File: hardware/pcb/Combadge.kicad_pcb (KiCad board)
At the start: 2 copper layers, 33.7 x 31 mm, 32 parts, among them J1 Conn_01x02_Female, J2 USB_B_Micro, J3 TOUCH, J4 Conn_01x02_Female, SW1 CSS-1210TB, U1 XC6808A4D28R-G, U2 ESP32-WROOM-32, U3 NCP160AMX330TBG, U4 MAX98357AEWL+T, U5 RN4989

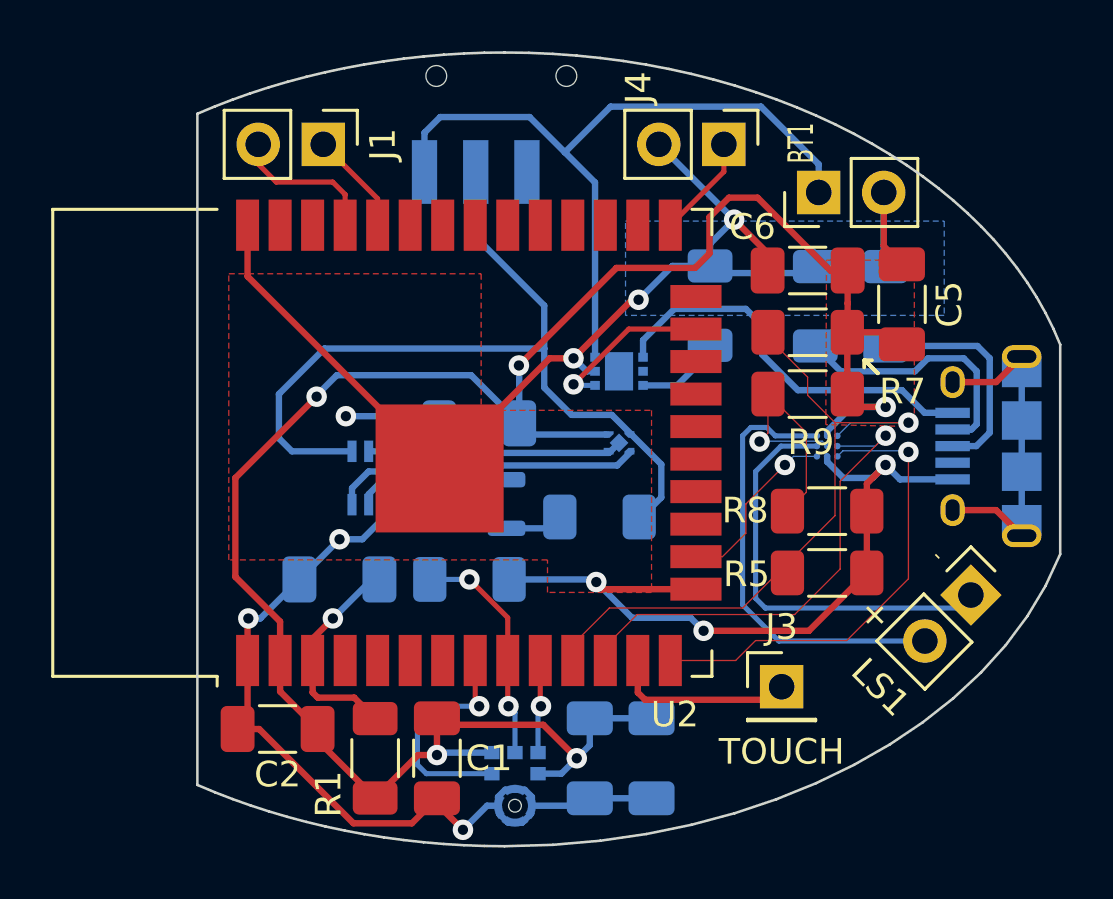
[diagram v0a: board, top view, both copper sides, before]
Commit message: Fix USP-6B07 footprint
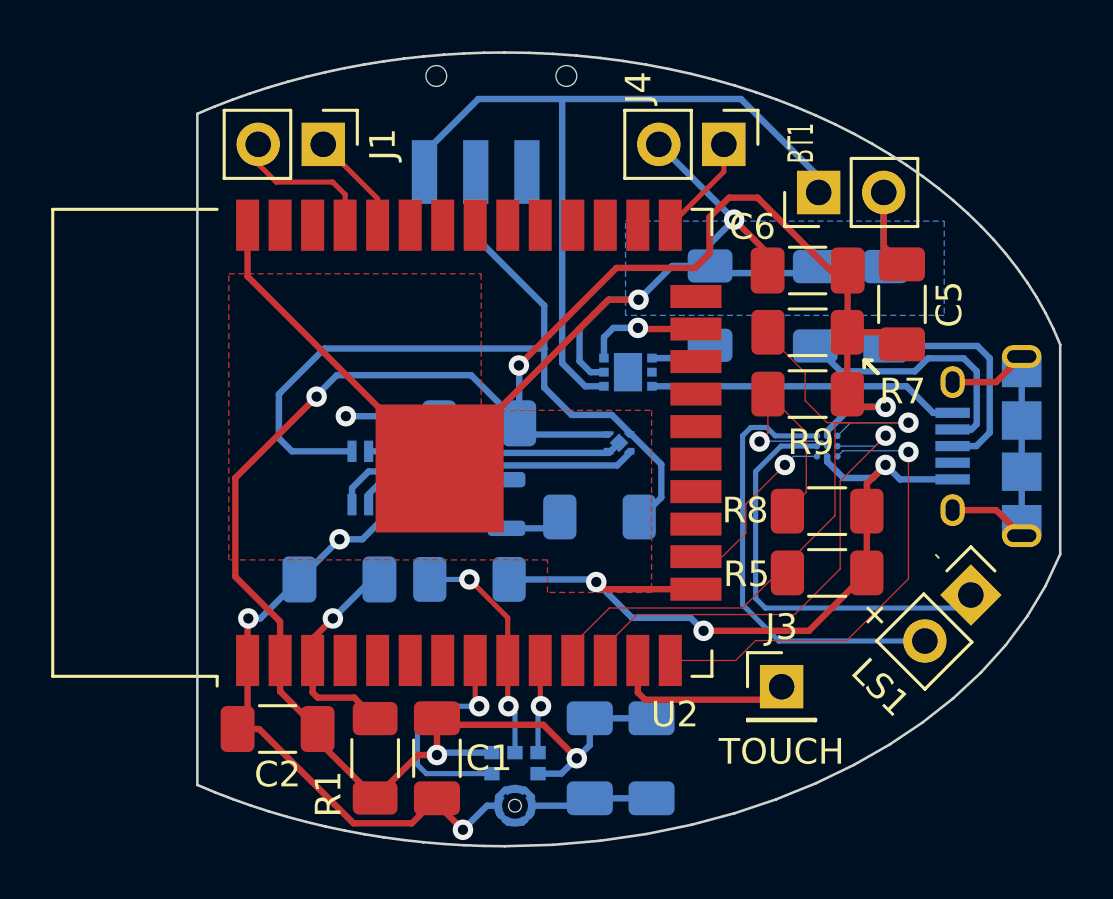
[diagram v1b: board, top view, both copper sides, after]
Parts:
- moved U1 0.35 mm to (160.8, 92.8), turned to 90 degrees
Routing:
- net GND: track 127.1 -> 131.2 mm, vias 10 -> 9
- net Net-(J2-Pad1): track 15.6 -> 12.2 mm
- net +BATT: track 29.0 -> 31.2 mm
- net /Power/CHRG_STATUS: track 6.53 -> 4.57 mm
- net /SPK_EN: track 27.3 -> 28.3 mm
- net Net-(R_ISET1-Pad2): track 3.15 -> 2.48 mm
- removed copper zone on F.Cu, net +3.3V

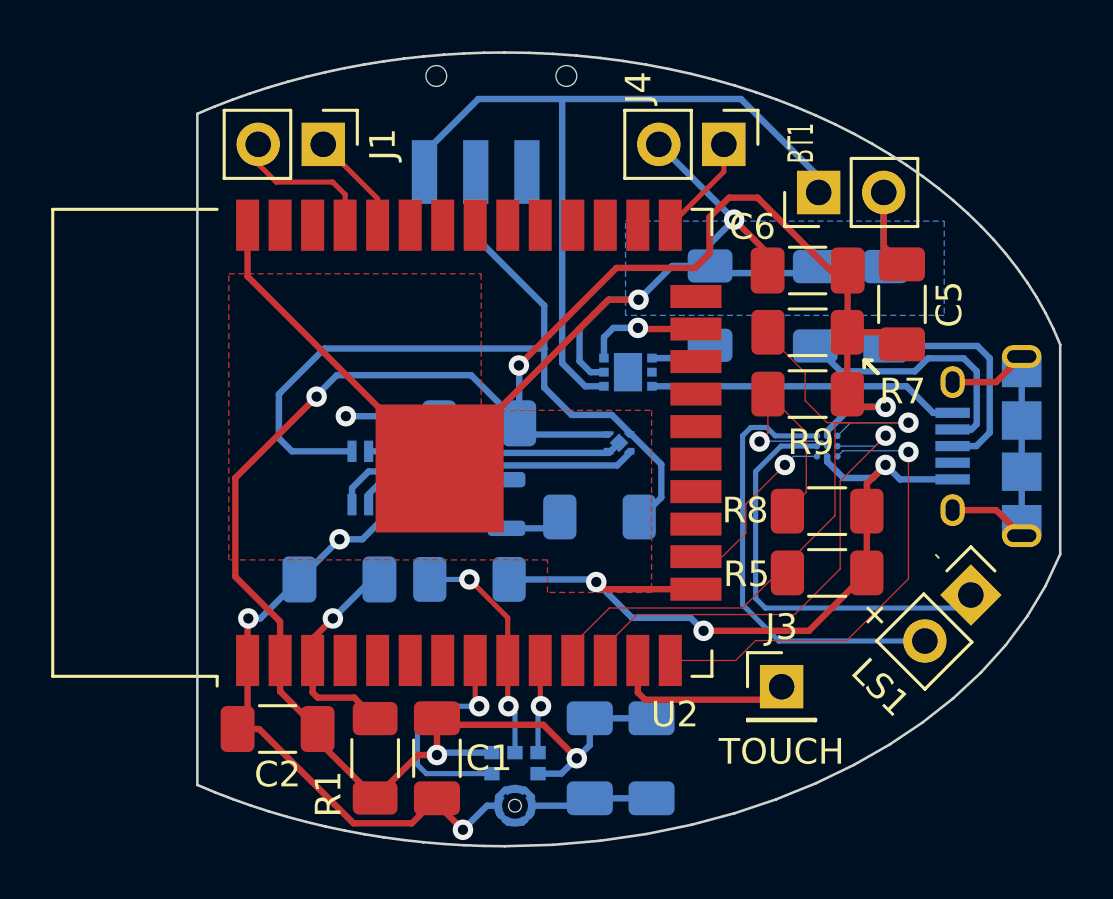
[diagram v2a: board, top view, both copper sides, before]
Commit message: Add MCP73831 to PCB
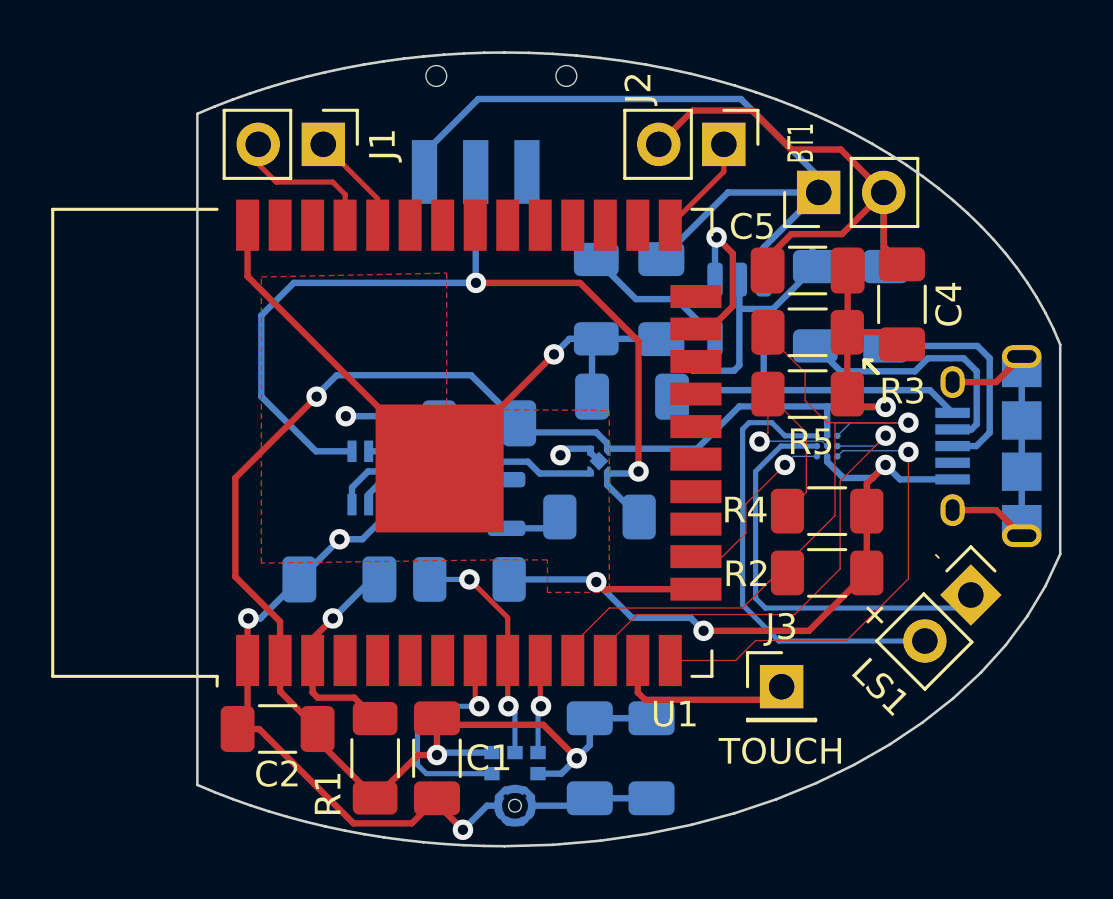
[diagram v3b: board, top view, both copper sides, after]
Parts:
- removed R_ISET1: 10k, Resistor_SMD:R_1206_3216Metric_Pad1.30x1.75mm_HandSolder
- removed the U1 at (160.8, 92.8)
- added C10: 4.7uF, Capacitor_SMD:C_1206_3216Metric_Pad1.33x1.80mm_HandSolder, B.Cu at (162.1, 89.9)
- added C9: 4.7uF, Capacitor_SMD:C_1206_3216Metric_Pad1.33x1.80mm_HandSolder, B.Cu at (160.9, 93.7)
- added R9: 4k, Resistor_SMD:R_1206_3216Metric_Pad1.30x1.75mm_HandSolder, B.Cu at (159.5, 89.9)
- added U3: MCP73831-2-OT, Package_TO_SOT_SMD:SOT-23-5, B.Cu at (165.1, 90.3)
- moved U5 1.06 mm to (159.6, 96.2), turned to 180 degrees
- renumbered C5 to C4, C6 to C5, C7 to C6, C8 to C7, C4 to C8, J4 to J2, J2 to J4, R4 to R10, R5 to R2, R7 to R3, R8 to R4, R9 to R5, R2 to R7, R3 to R8, U2 to U1, U4 to U2, U5 to U4, U3 to U5
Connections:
- net Net-(U4-GAIN_SLOT) renamed /GAIN_SELECT
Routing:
- net +3.3V: track 82.2 -> 72.6 mm, vias 5 -> 4
- net Net-(U3-PROG): track 0.00 -> 5.91 mm
- net Net-(U4-EMITTER2): track 33.7 -> 36.7 mm, vias 0 -> 2
- net Net-(U1-ISET): track 2.48 -> 0.00 mm
- net /Power/CHRG_STATUS: track 4.57 -> 6.44 mm
- net GND: track 131.2 -> 133.0 mm
- net Net-(U4-COLLECTOR2): track 12.2 -> 10.6 mm
- net Net-(J4-VBUS): track 12.2 -> 13.5 mm
- net +BATT: track 31.2 -> 30.4 mm
- removed copper zone on B.Cu, net GND

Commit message: Use single resistor for setting amplifier gain
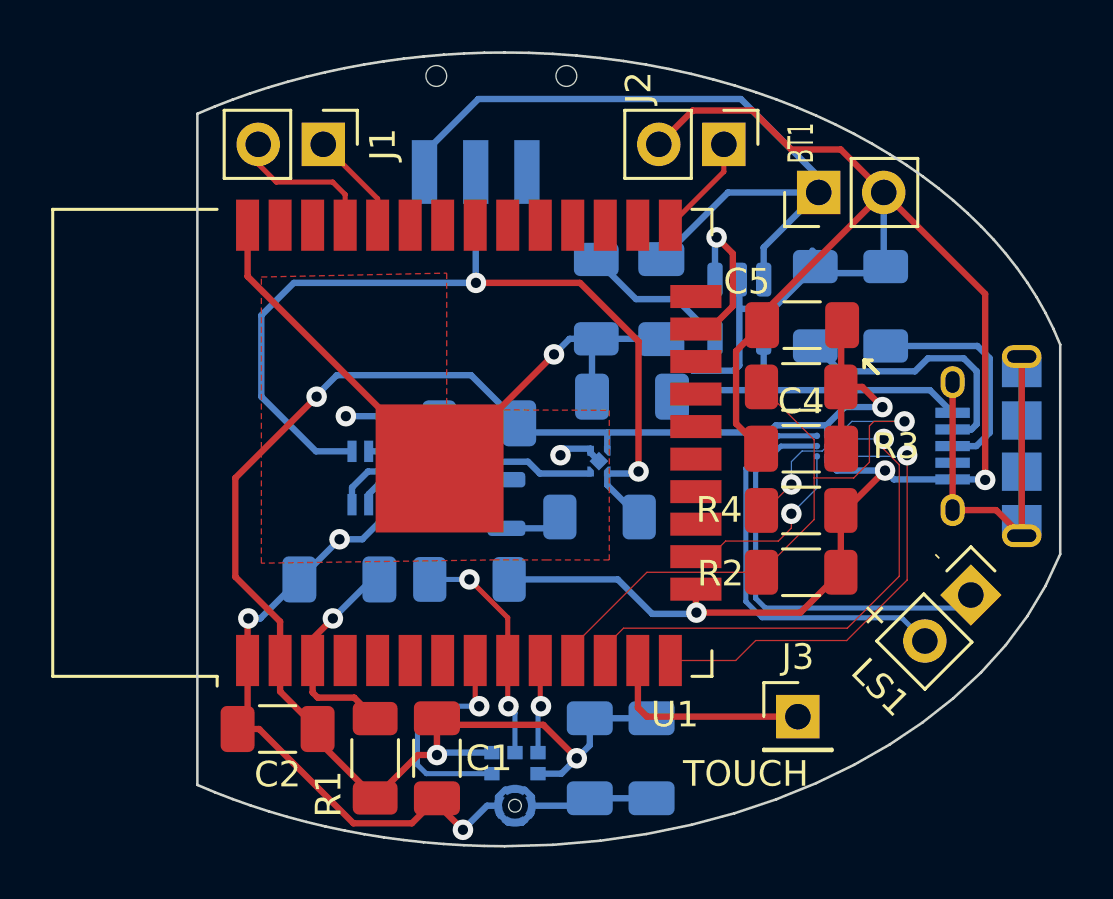
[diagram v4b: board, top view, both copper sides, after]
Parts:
- removed the R5 at (167.8, 93.6)
- R4: value TBD -> 100k
- moved C4 6.88 mm to (167.5, 95.8), turned to 0 degrees
- moved R3 2.15 mm to (167.5, 93.3)
- moved C5 2.14 mm to (167.6, 90.9)
- moved J3 1.33 mm to (167.4, 106.2)
- moved R2 1.02 mm to (167.5, 100.6)
- moved R4 1.02 mm to (167.5, 98.2)
- renumbered C8 to C10, C9 to C8, C10 to C9, R6 to R5, R7 to R6, R8 to R7, R9 to R8, R10 to R9
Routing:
- net GND: track 133.0 -> 146.1 mm
- net unconnected-(J4-Shield-Pad6): track 12.0 -> 20.9 mm
- net /GAIN_SELECT: track 10.2 -> 4.13 mm
- net +3.3V: track 72.6 -> 69.6 mm
- net /SPK_EN: track 28.3 -> 26.2 mm
- net /SPK_DATA: track 19.0 -> 20.7 mm
- net /SPK+: track 17.8 -> 16.1 mm
- net Net-(J3-Pin_1): track 7.19 -> 8.23 mm

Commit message: Cleanup silkscreen
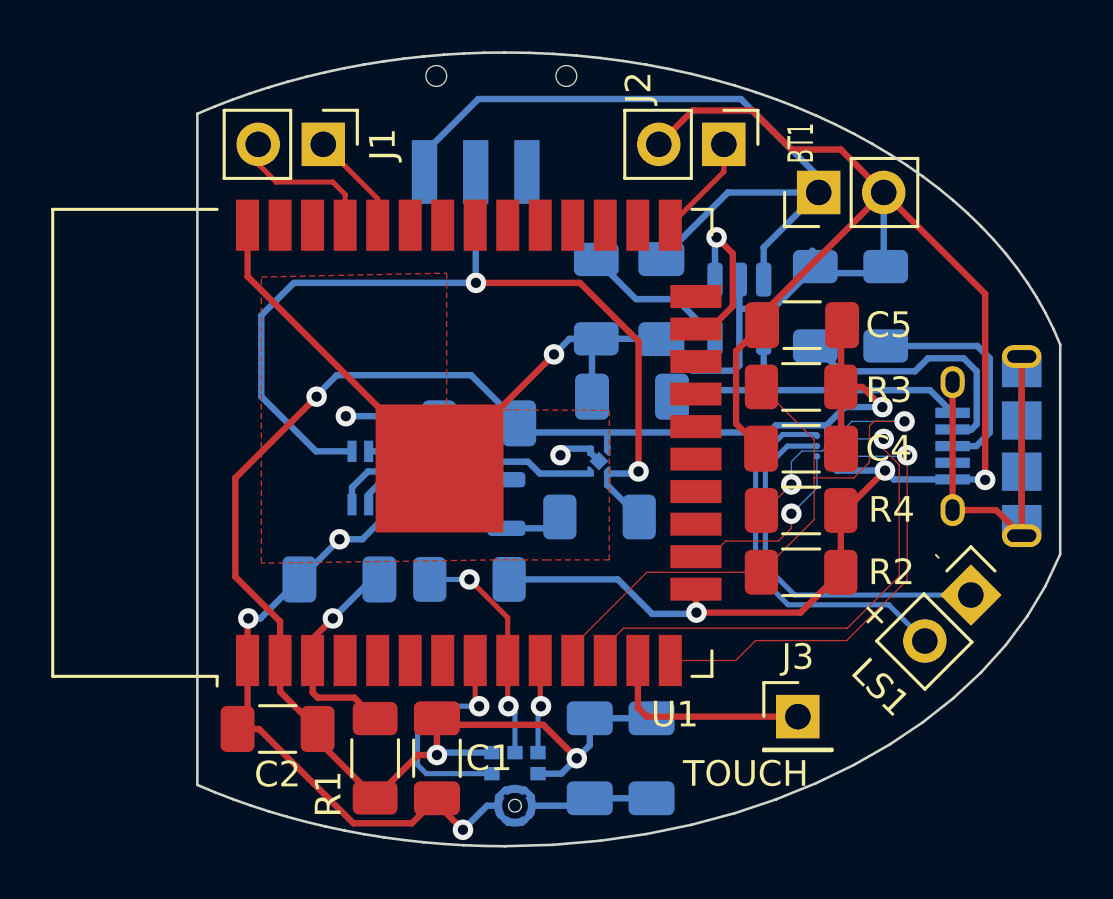
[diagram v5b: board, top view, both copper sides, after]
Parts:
- U2: value MAX98357AEWL+T -> MAX98357
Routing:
- net /SPK+: track 16.1 -> 14.9 mm
- net /SPK-: track 16.5 -> 15.4 mm
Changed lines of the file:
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@@
     (property "ki_keywords" "cap capacitor")
     (attr smd)
-    (fp_text reference "C4" (at 0 -1.85) (layer "F.SilkS")
+    (fp_text reference "C4" (at 3.429 0) (layer "F.SilkS")
         (effects (font (size 1 1) (thickness 0.15)))
     )
@@
     (property "ki_keywords" "R res resistor")
     (attr smd)
-    (fp_text reference "R3" (at -3.7084 -2.3114) (layer "F.SilkS")
+    (fp_text reference "R3" (at -3.429 -0.127) (layer "F.SilkS")
         (effects (font (size 1 1) (thickness 0.15)))
     )
@@
     (property "ki_keywords" "cap capacitor")
     (attr smd)
-    (fp_text reference "C5" (at -2.159 -1.7018) (layer "F.SilkS")
+    (fp_text reference "C5" (at 3.3905 0) (layer "F.SilkS")
         (effects (font (size 1 1) (thickness 0.15)))
     )
@@
     (property "ki_keywords" "R res resistor")
     (attr smd)
-    (fp_text reference "R4" (at -3.2004 -0.0254) (layer "F.SilkS")
+    (fp_text reference "R4" (at 3.5306 -0.0254) (layer "F.SilkS")
         (effects (font (size 1 1) (thickness 0.15)))
     )
@@
     (property "ki_keywords" "R res resistor")
     (attr smd)
-    (fp_text reference "R2" (at 3.1496 -0.0508) (layer "F.SilkS")
+    (fp_text reference "R2" (at -3.5306 0) (layer "F.SilkS")
         (effects (font (size 1 1) (thickness 0.15)))
     )
@@
     (property "ki_keywords" "cap capacitor")
     (attr smd)
-    (fp_text reference "C9" (at 0 1.85 90) (layer "B.SilkS")
-        (effects (font (size 1 1) (thickness 0.15)) (justify mirror))
+    (fp_text reference "C9" (at -2.921 -1.143 90) (layer "B.SilkS")
+        (effects (font (size 0.5 0.5) (thickness 0.125)) (justify mirror))
     )
     (fp_text value "4.7uF" (at 0 -1.85 90) (layer "B.Fab")
@@
     (property "ki_keywords" "battery charger lithium")
     (attr smd)
-    (fp_text reference "U3" (at 0 2.4 90) (layer "B.SilkS")
+    (fp_text reference "U3" (at 2.9265 0 90) (layer "B.SilkS")
         (effects (font (size 1 1) (thickness 0.15)) (justify mirror))
     )
@@
     (property "ki_keywords" "R res resistor")
     (attr smd)
-    (fp_text reference "R7" (at 0 -1.824 90) (layer "B.SilkS")
-        (effects (font (size 1 1) (thickness 0.15)) (justify mirror))
+    (fp_text reference "R7" (at -3.0226 0.081 90) (layer "B.SilkS")
+        (effects (font (size 0.5 0.5) (thickness 0.125)) (justify mirror))
     )
     (fp_text value "10k" (at 0 -1.82 90) (layer "B.Fab")
@@
     (property "ki_keywords" "cap capacitor")
     (attr smd)
-    (fp_text reference "C8" (at 0 1.85) (layer "B.SilkS")
-        (effects (font (size 1 1) (thickness 0.15)) (justify mirror))
+    (fp_text reference "C8" (at -2.794 -1.397) (layer "B.SilkS")
+        (effects (font (size 0.5 0.5) (thickness 0.125)) (justify mirror))
     )
     (fp_text value "4.7uF" (at 0 -1.85) (layer "B.Fab")
@@
         (effects (font (size 1 1) (thickness 0.15)) (justify mirror))
     )
-    (fp_text value "MAX98357AEWL+T" (at 0 -1.3462) (layer "B.SilkS")
+    (fp_text value "MAX98357" (at 0 -1.3462) (layer "B.SilkS")
         (effects (font (size 0.4 0.4) (thickness 0.05)) (justify mirror))
     )
@@
     (property "ki_keywords" "R res resistor")
     (attr smd)
-    (fp_text reference "R6" (at -1.1176 1.566 90) (layer "B.SilkS")
+    (fp_text reference "R6" (at 0.0254 1.905 90) (layer "B.SilkS")
         (effects (font (size 1 1) (thickness 0.15)) (justify mirror))
     )
@@
     (property "Sheetname" "Power")
     (attr smd)
-    (fp_text reference "U5" (at 0.04 1.778) (layer "B.SilkS")
+    (fp_text reference "U5" (at -1.928 -0.023) (layer "B.SilkS")
         (effects (font (size 1 1) (thickness 0.15)) (justify mirror))
     )
@@
     (property "ki_keywords" "R res resistor")
     (attr smd)
-    (fp_text reference "R8" (at 0 1.82 90) (layer "B.SilkS")
+    (fp_text reference "R8" (at 0 1.778 90) (layer "B.SilkS")
         (effects (font (size 1 1) (thickness 0.15)) (justify mirror))
     )
@@
     )
   )
-  (gr_line (start 170.0022 92.3036) (end 170.5102 92.8116)
-    (stroke (width 0.15) (type solid)) (layer "F.SilkS"))
-  (gr_line (start 170.5102 92.8116) (end 170.0022 92.3036)
-    (stroke (width 0.15) (type solid)) (layer "F.SilkS"))
-  (gr_line (start 169.9768 92.3036) (end 170.2816 92.3036)
-    (stroke (width 0.15) (type solid)) (layer "F.SilkS"))
-  (gr_line (start 169.9768 92.3036) (end 169.9768 92.583)
-    (stroke (width 0.15) (type solid)) (layer "F.SilkS"))
   (gr_poly
     (pts
@@
   (segment (start 154.803475 89.271475) (end 154.803475 84.9503) (width 0.25) (layer "B.Cu") (net 26))
   (segment (start 146.431 90.551) (end 147.701 89.281) (width 0.25) (layer "B.Cu") (net 26))
-  (segment (start 165.735 101.6) (end 166.116 101.981) (width 0.2) (layer "B.Cu") (net 44))
-  (segment (start 166.7256 95.6564) (end 165.735 96.647) (width 0.2) (layer "B.Cu") (net 44))
-  (segment (start 165.735 96.647) (end 165.735 101.6) (width 0.2) (layer "B.Cu") (net 44))
-  (segment (start 166.116 101.981) (end 173.6344 101.981) (width 0.2) (layer "B.Cu") (net 44))
+  (segment (start 166.116 96.52) (end 166.116 100.33) (width 0.2) (layer "B.Cu") (net 44))
+  (segment (start 168.129 95.6564) (end 166.9796 95.6564) (width 0.2) (layer "B.Cu") (net 44))
   (segment (start 173.6344 101.981) (end 174.1424 101.473) (width 0.2) (layer "B.Cu") (net 44))
-  (segment (start 168.129 95.6564) (end 166.7256 95.6564) (width 0.2) (layer "B.Cu") (net 44))
-  (segment (start 171.439298 102.362) (end 172.346349 103.269051) (width 0.2) (layer "B.Cu") (net 45))
-  (segment (start 168.129 95.2564) (end 166.6176 95.2564) (width 0.2) (layer "B.Cu") (net 45))
-  (segment (start 165.989 102.362) (end 171.439298 102.362) (width 0.2) (layer "B.Cu") (net 45))
-  (segment (start 165.354 96.52) (end 165.354 101.727) (width 0.2) (layer "B.Cu") (net 45))
-  (segment (start 166.6176 95.2564) (end 165.354 96.52) (width 0.2) (layer "B.Cu") (net 45))
-  (segment (start 165.354 101.727) (end 165.989 102.362) (width 0.2) (layer "B.Cu") (net 45))
+  (segment (start 167.259 101.473) (end 174.1424 101.473) (width 0.2) (layer "B.Cu") (net 44))
+  (segment (start 166.9796 95.6564) (end 166.116 96.52) (width 0.2) (layer "B.Cu") (net 44))
+  (segment (start 166.116 100.33) (end 167.259 101.473) (width 0.2) (layer "B.Cu") (net 44))
+  (segment (start 168.129 95.231) (end 168.098898 95.200898) (width 0.2) (layer "B.Cu") (net 45))
+  (segment (start 167.005 101.854) (end 170.942 101.854) (width 0.2) (layer "B.Cu") (net 45))
+  (segment (start 166.800102 95.200898) (end 165.735 96.266) (width 0.2) (layer "B.Cu") (net 45))
+  (segment (start 170.942 101.864702) (end 172.346349 103.269051) (width 0.2) (layer "B.Cu") (net 45))
+  (segment (start 165.735 100.584) (end 167.005 101.854) (width 0.2) (layer "B.Cu") (net 45))
+  (segment (start 168.129 95.2564) (end 168.129 95.231) (width 0.2) (layer "B.Cu") (net 45))
+  (segment (start 165.735 96.266) (end 165.735 100.584) (width 0.2) (layer "B.Cu") (net 45))
+  (segment (start 170.942 101.854) (end 170.942 101.864702) (width 0.2) (layer "B.Cu") (net 45))
+  (segment (start 168.098898 95.200898) (end 166.800102 95.200898) (width 0.2) (layer "B.Cu") (net 45))
   (segment (start 152.908 96.266) (end 152.527 96.647) (width 0.25) (layer "B.Cu") (net 51))
   (segment (start 156.845 96.266) (end 152.908 96.266) (width 0.25) (layer "B.Cu") (net 51))
